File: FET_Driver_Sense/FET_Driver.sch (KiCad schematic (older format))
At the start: 16 parts, among them J101 Interface, J102 Out, Q101 IRF5210SPbF, U101 EL3H7(C)(TA)-G, U102 ACS712xLCTR-20A, U603 H7550-H#

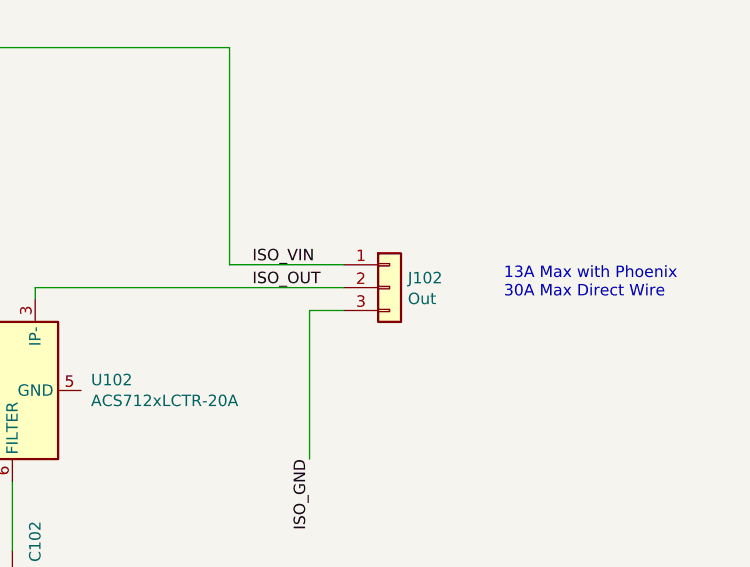
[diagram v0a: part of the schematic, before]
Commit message: Opto Tacho (Schmidtt),   Fixes to FET_Driver_Sense
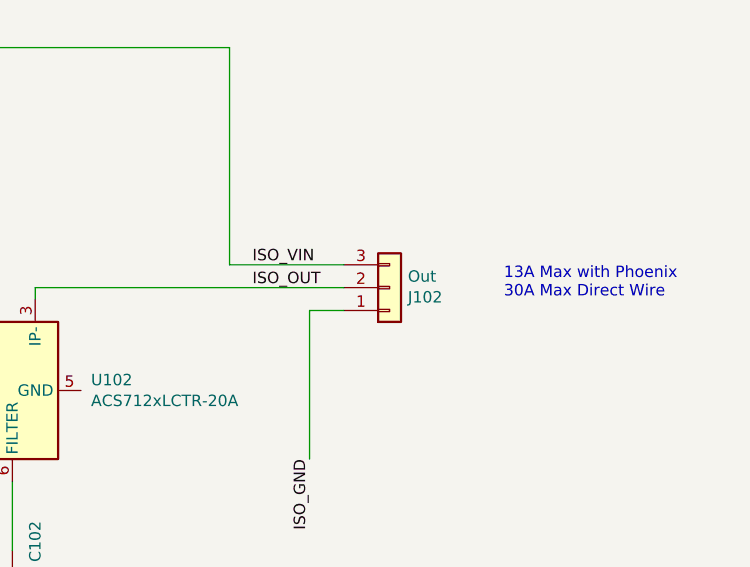
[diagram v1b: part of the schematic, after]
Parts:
- J102: footprint Connector_Phoenix_MC:PhoenixContact_MCV_1,5_3-G-3.81_1x03_P3.81mm_Vertical -> Connector_Phoenix_MC:PhoenixContact_MC_1,5_3-G-3.81_1x03_P3.81mm_Horizontal
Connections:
- net ISO_GND: now also J102.1 (Pin_1); no longer J102.3 (Pin_3)
- net ISO_VIN: now also J102.3 (Pin_3); no longer J102.1 (Pin_1)
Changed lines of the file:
@@
 F 0 "J102" H 9030 3142 50  0000 L CNN
 F 1 "Out" H 9030 3051 50  0000 L CNN
-F 2 "Connector_Phoenix_MC:PhoenixContact_MCV_1,5_3-G-3.81_1x03_P3.81mm_Vertical" H 8950 3100 50  0001 C CNN
+F 2 "Connector_Phoenix_MC:PhoenixContact_MC_1,5_3-G-3.81_1x03_P3.81mm_Horizontal" H 8950 3100 50  0001 C CNN
 F 3 "~" H 8950 3100 50  0001 C CNN
 	1    8950 3100
-	1    0    0    -1
+	1    0    0    1
 $EndComp
 $Comp

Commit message: Fix Symbol Libraries
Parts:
- Q101: symbol FET_Driver:IRF5210SPbF -> YachtHardware:IRF5210SPbF
- U101: symbol SH-ESP32:EL3H7 -> YachtHardware:EL3H7
- U603: symbol SH-ESP32:HT75xx-1-SOT23 -> YachtHardware:HT75xx-1-SOT23
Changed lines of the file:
@@
 GPIO
 $Comp
-L FET_Driver:IRF5210SPbF Q101
+L YachtHardware:IRF5210SPbF Q101
 U 1 1 5FB80F51
 P 5050 2850
@@
 Flyback diode for \ninductive loads
 $Comp
-L SH-ESP32:EL3H7 U101
+L YachtHardware:EL3H7 U101
 U 1 1 5FCB38F6
 P 3650 2950
@@
 	4150 5550 4150 5400
 $Comp
-L SH-ESP32:HT75xx-1-SOT23 U?
+L YachtHardware:HT75xx-1-SOT23 U?
 U 1 1 5F94C95C
 P 4150 4900

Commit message: FET Driver - LCSC Parts tidy up
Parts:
- added D502: GREEN LED, LED_SMD:LED_0603_1608Metric, symbol Device:LED
- added R502: 2k, Resistor_SMD:R_0402_1005Metric, symbol Device:R
- Q101: value IRF5210SPbF -> IRF5210STRLPBF; LCSC (none) -> C2622
- R101, R103: LCSC (none) -> C25804
- R102: LCSC (none) -> C21190
- R104: LCSC (none) -> C22975
- U102: value ACS712xLCTR-20A -> ACS712ELCTR-20A-T; LCSC (none) -> C10681
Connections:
- wire segments 67 -> 71
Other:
- note removed: "Input voltage up to 40V"
- moved on the sheet: C101, C102, C603, C605, D101, J102, R101, R102, R103, R104, R901, U102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
